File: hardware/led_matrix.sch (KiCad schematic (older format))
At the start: 22 parts, among them U10 SM16106, U11 SM16106, U9 SM16106

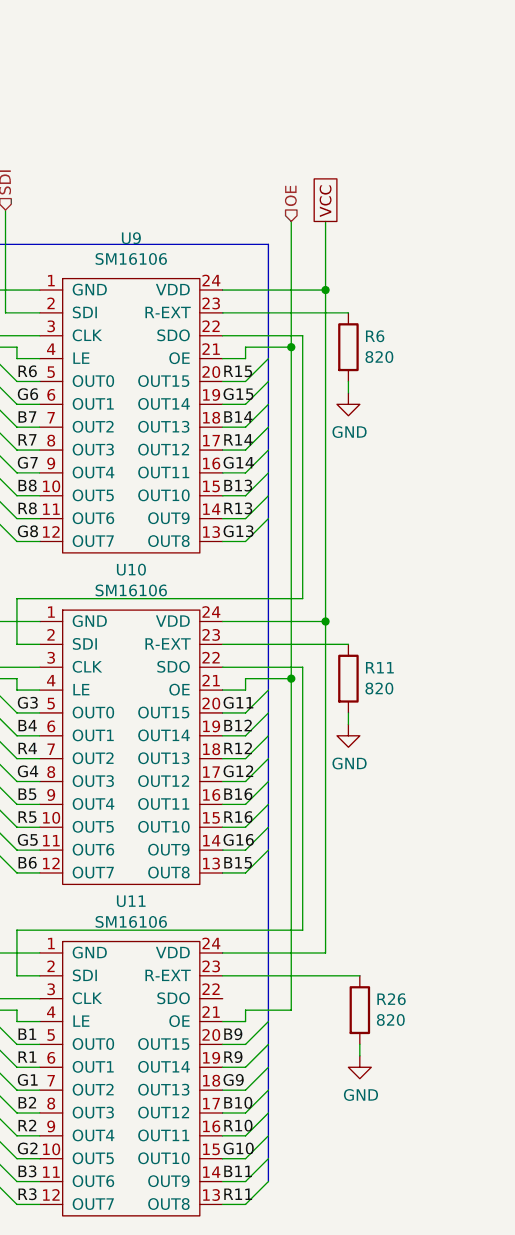
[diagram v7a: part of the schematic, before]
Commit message: Fixed 3.3V rail to led drivers. Switched to 2A diode
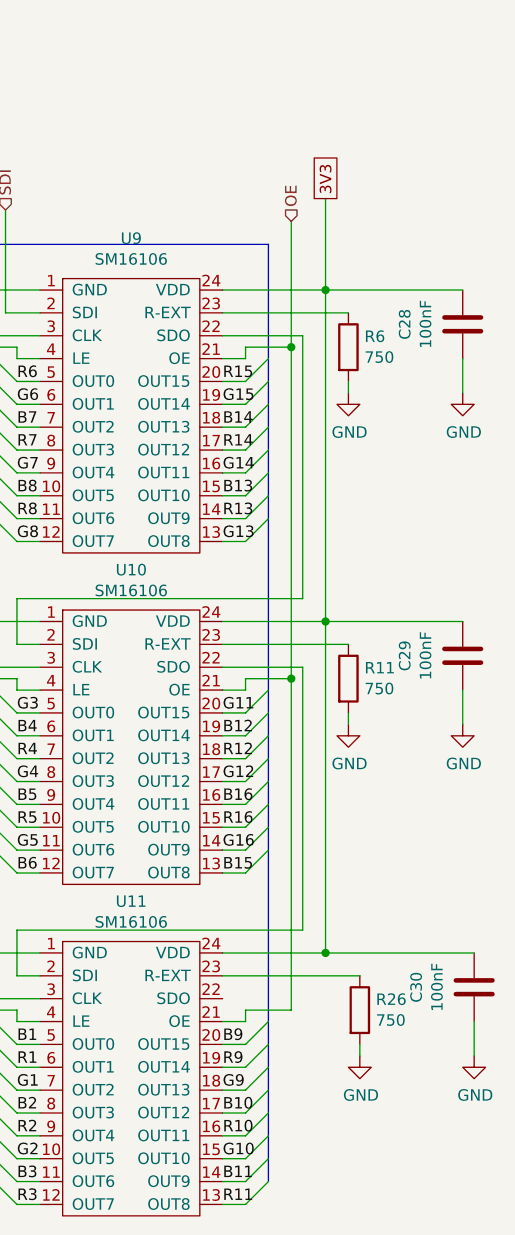
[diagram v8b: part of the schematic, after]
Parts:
- added C28, C29, C30: 100nF, Capacitor_SMD:C_0603_1608Metric, symbol Device:C
- R11, R26, R6: value 820 -> 750; LCSC C23253 -> (none)
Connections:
- net GND: now also C28.2, C29.2, C30.2
- net VCC: no longer U10.24 (VDD), U11.24 (VDD), U9.24 (VDD)
- new net 3V3: C28.1, C29.1, C30.1, U10.24 (VDD), U11.24 (VDD), U9.24 (VDD)
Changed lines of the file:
@@
 Text HLabel 7200 1650 1    50   Input ~ 0
 SDI
-Text GLabel 8600 1700 1    50   UnSpc ~ 0
-VCC
 Wire Wire Line
 	8150 2000 8600 2000
-Wire Wire Line
-	8600 2000 8600 1700
 Wire Wire Line
 	8600 2000 8600 3450
@@
 P 8750 5150
 F 0 "R26" H 8820 5196 50  0000 L CNN
-F 1 "820" H 8820 5105 50  0000 L CNN
+F 1 "750" H 8820 5105 50  0000 L CNN
 F 2 "Resistor_SMD:R_0603_1608Metric" V 8680 5150 50  0001 C CNN
 F 3 "~" H 8750 5150 50  0001 C CNN
-F 4 "C23253" H 8750 5150 50  0001 C CNN "LCSC"
+F 4 "" H 8750 5150 50  0001 C CNN "LCSC"
 	1    8750 5150
 	1    0    0    -1
@@
 P 8700 3700
 F 0 "R11" H 8770 3746 50  0000 L CNN
-F 1 "820" H 8770 3655 50  0000 L CNN
+F 1 "750" H 8770 3655 50  0000 L CNN
 F 2 "Resistor_SMD:R_0603_1608Metric" V 8630 3700 50  0001 C CNN
 F 3 "~" H 8700 3700 50  0001 C CNN
-F 4 "C23253" H 8700 3700 50  0001 C CNN "LCSC"
+F 4 "" H 8700 3700 50  0001 C CNN "LCSC"
 	1    8700 3700
 	1    0    0    -1
@@
 P 8700 2250
 F 0 "R6" H 8770 2296 50  0000 L CNN
-F 1 "820" H 8770 2205 50  0000 L CNN
+F 1 "750" H 8770 2205 50  0000 L CNN
 F 2 "Resistor_SMD:R_0603_1608Metric" V 8630 2250 50  0001 C CNN
 F 3 "~" H 8700 2250 50  0001 C CNN
-F 4 "C23253" H 8700 2250 50  0001 C CNN "LCSC"
+F 4 "" H 8700 2250 50  0001 C CNN "LCSC"
 	1    8700 2250
 	1    0    0    -1
@@
 	0    -1   -1   0
 $EndComp
+Text GLabel 8600 1600 1    50   UnSpc ~ 0
+3V3
+Wire Wire Line
+	8600 1600 8600 2000
+$Comp
+L Device:C C?
+U 1 1 5EC6B7FF
+P 9200 2150
+AR Path="/5DC753C3/5EC6B7FF" Ref="C?"  Part="1"
+AR Path="/5EC6B7FF" Ref="C?"  Part="1"
+AR Path="/5E7D231B/5EC6B7FF" Ref="C28"  Part="1"
+F 0 "C28" V 8948 2150 50  0000 C CNN
+F 1 "100nF" V 9039 2150 50  0000 C CNN
+F 2 "Capacitor_SMD:C_0603_1608Metric" H 9238 2000 50  0001 C CNN
+F 3 "~" H 9200 2150 50  0001 C CNN
+F 4 "C14663" H 9200 2150 50  0001 C CNN "LCSC"
+	1    9200 2150
+	1    0    0    -1
+$EndComp
+$Comp
+L Device:C C?
+U 1 1 5EC7417D
+P 9200 3600
+AR Path="/5DC753C3/5EC7417D" Ref="C?"  Part="1"
+AR Path="/5EC7417D" Ref="C?"  Part="1"
+AR Path="/5E7D231B/5EC7417D" Ref="C29"  Part="1"
+F 0 "C29" V 8948 3600 50  0000 C CNN
+F 1 "100nF" V 9039 3600 50  0000 C CNN
+F 2 "Capacitor_SMD:C_0603_1608Metric" H 9238 3450 50  0001 C CNN
+F 3 "~" H 9200 3600 50  0001 C CNN
+F 4 "C14663" H 9200 3600 50  0001 C CNN "LCSC"
+	1    9200 3600
+	1    0    0    -1
+$EndComp
+Wire Wire Line
+	8600 3450 9200 3450
+$Comp
+L power:GND #PWR0105
+U 1 1 5EC83ACB
+P 9200 3900
+F 0 "#PWR0105" H 9200 3650 50  0001 C CNN
+F 1 "GND" H 9205 3727 50  0000 C CNN
+F 2 "" H 9200 3900 50  0001 C CNN
+F 3 "" H 9200 3900 50  0001 C CNN
+	1    9200 3900
+	1    0    0    -1
+$EndComp
+Wire Wire Line
+	9200 3900 9200 3750
+$Comp
+L power:GND #PWR0106
+U 1 1 5EC8BF56
+P 9200 2450
+F 0 "#PWR0106" H 9200 2200 50  0001 C CNN
+F 1 "GND" H 9205 2277 50  0000 C CNN
+F 2 "" H 9200 2450 50  0001 C CNN
+F 3 "" H 9200 2450 50  0001 C CNN
+	1    9200 2450
+	1    0    0    -1
+$EndComp
+Wire Wire Line
+	9200 2450 9200 2300
+Wire Wire Line
+	9200 2000 8600 2000
+$Comp
+L Device:C C?
+U 1 1 5EC9D39D
+P 9250 5050
+AR Path="/5DC753C3/5EC9D39D" Ref="C?"  Part="1"
+AR Path="/5EC9D39D" Ref="C?"  Part="1"
+AR Path="/5E7D231B/5EC9D39D" Ref="C30"  Part="1"
+F 0 "C30" V 8998 5050 50  0000 C CNN
+F 1 "100nF" V 9089 5050 50  0000 C CNN
+F 2 "Capacitor_SMD:C_0603_1608Metric" H 9288 4900 50  0001 C CNN
+F 3 "~" H 9250 5050 50  0001 C CNN
+F 4 "C14663" H 9250 5050 50  0001 C CNN "LCSC"
+	1    9250 5050
+	1    0    0    -1
+$EndComp
+Wire Wire Line
+	8600 4900 9250 4900
+Connection ~ 8600 4900
+$Comp
+L power:GND #PWR0107
+U 1 1 5ECA7297
+P 9250 5350
+F 0 "#PWR0107" H 9250 5100 50  0001 C CNN
+F 1 "GND" H 9255 5177 50  0000 C CNN
+F 2 "" H 9250 5350 50  0001 C CNN
+F 3 "" H 9250 5350 50  0001 C CNN
+	1    9250 5350
+	1    0    0    -1
+$EndComp
+Wire Wire Line
+	9250 5350 9250 5200
 Wire Bus Line
 	3050 1800 6150 1800
